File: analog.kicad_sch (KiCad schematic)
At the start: 47 parts, among them J8 Sensor harness, U7 ADS1115-Q1

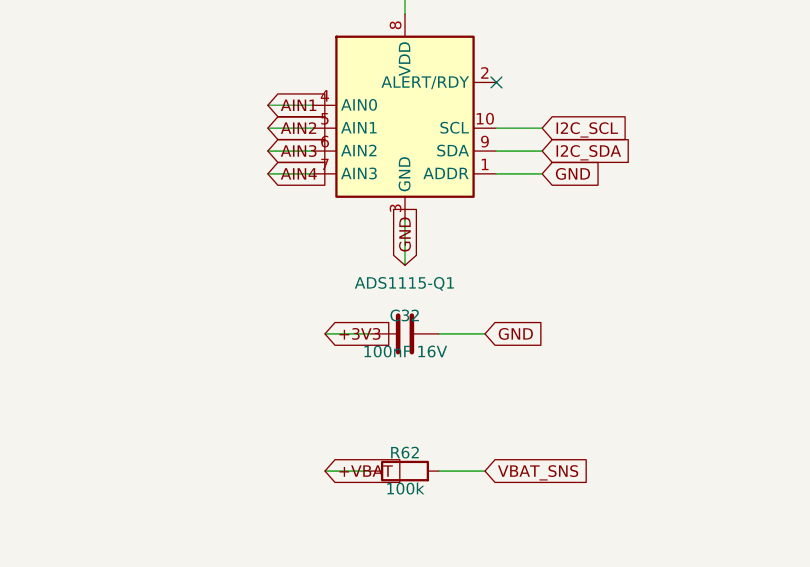
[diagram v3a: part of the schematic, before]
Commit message: Source the BOM for JLCPCB assembly; fix a nonexistent FET part number
Availability check against LCSC / DigiKey / Mouser (2026-08), with the
board now targeted at JLCPCB pick-and-place:

- Q1 was specified as PSMN4R3-100BSE, a part number that does not exist
  (Nexperia's nearest real part is the D2PAK PSMN4R8-100BSE, which would
  not fit the TO-252 footprint anyway). Replaced with Infineon
  IPD068N10N3G (LCSC C88066): DPAK, 100V, 6.8mOhm, in stock.
- LM5164QDDARQ1 is backordered at DigiKey and nearly dry at Mouser;
  switched to the non-automotive LM5164DDAR (LCSC C477928, DigiKey 3.4k
  in stock). Same silicon, minus AEC-Q100.
- ADS1115QDGSRQ1 requires a manufacturer quote at DigiKey; switched to
  ADS1115IDGSR (LCSC C37593, in stock).

README gains a sourcing table with LCSC part numbers for the critical
semiconductors and a list of what still gets picked from the live JLC
catalog at layout time (buck inductors, bulk electrolytic, 0.1%
resistors).

Validated with kicad-cli 9.0: 104 nets / 162 instances match, ERC clean.

Co-Authored-By: Claude Fable 5 <noreply@anthropic.com>
Claude-Session: https://claude.ai/code/session_01DhNbL25h25p8VFCjRfJik9
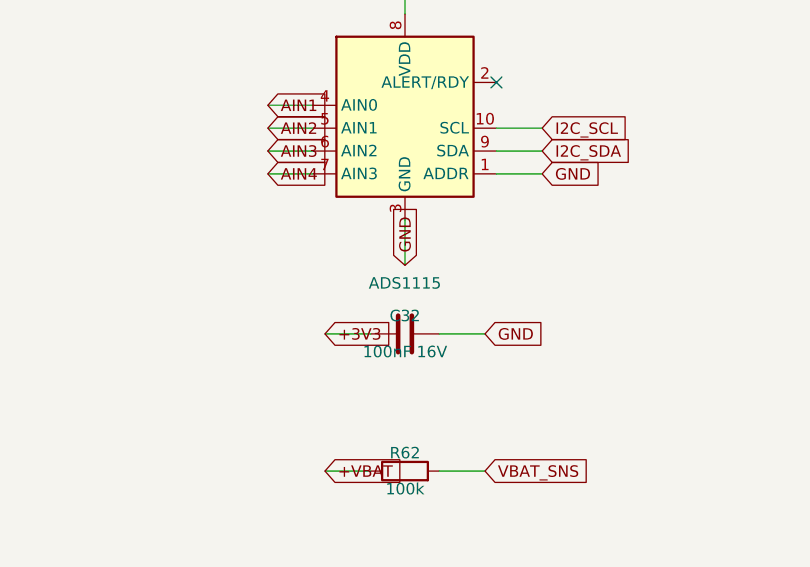
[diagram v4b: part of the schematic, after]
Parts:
- U7: value ADS1115-Q1 -> ADS1115; MPN ADS1115QDGSRQ1 -> ADS1115IDGSR
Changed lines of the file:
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@@
       (effects (font (size 1.27 1.27)) )
     )
-    (property "Value" "ADS1115-Q1" (at 241.3 209.01 0)
+    (property "Value" "ADS1115" (at 241.3 209.01 0)
       (effects (font (size 1.27 1.27)) )
     )
@@
       (effects (font (size 1.27 1.27)) hide)
     )
-    (property "MPN" "ADS1115QDGSRQ1" (at 241.3 209.01 0)
+    (property "MPN" "ADS1115IDGSR" (at 241.3 209.01 0)
       (effects (font (size 1.27 1.27)) hide)
     )

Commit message: Generate the 4-layer board: placed, DRC-clean, ready to route
gen/generate_pcb.py (runs under KiCad 9's bundled Python) builds
esp32s3-can-sd-logger.kicad_pcb from the same part/net tables as the
schematic generator: real library footprints, every pad netted, and
zone-based placement -- harness connectors on the left edge, analog
channel columns and the ESP32 with its antenna overhanging the top edge
(module keepout falls off-board), USB-C/microSD/buttons on the right,
battery front end and both bucks in the bottom band, GND and +3V3
inner-plane zones, JLC-compatible 0.2mm minimum drill.

84 x 72 mm. kicad-cli pcb drc: zero violations; the 335 unconnected
items are the unrouted ratsnest.

Also adds the project footprint library (TDK ACT45B CAN choke built from
the datasheet land pattern) and a placement render under plots/.

Co-Authored-By: Claude Fable 5 <noreply@anthropic.com>
Claude-Session: https://claude.ai/code/session_01DhNbL25h25p8VFCjRfJik9
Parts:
- J8: MPN JST B8B-PH-K -> JST B8B-PH-K-S(LF)(SN)
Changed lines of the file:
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@@
       (effects (font (size 1.27 1.27)) hide)
     )
-    (property "MPN" "JST B8B-PH-K" (at 54.61 37.56 0)
+    (property "MPN" "JST B8B-PH-K-S(LF)(SN)" (at 54.61 37.56 0)
       (effects (font (size 1.27 1.27)) hide)
     )

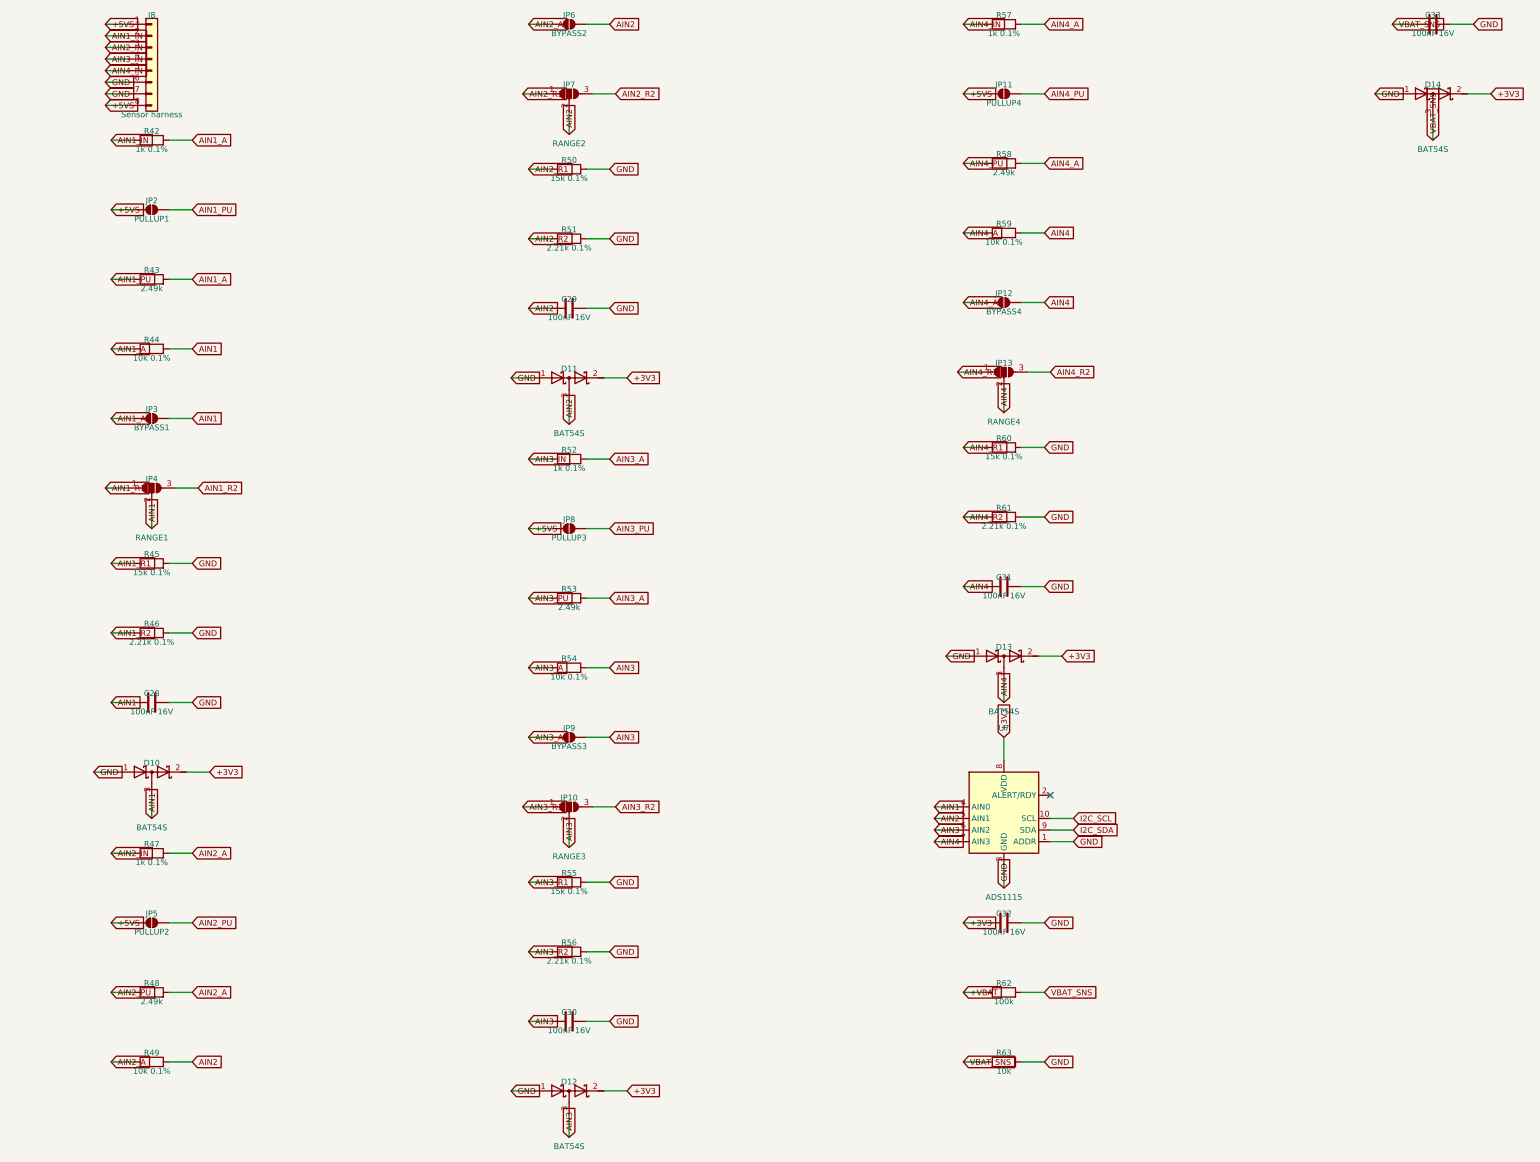
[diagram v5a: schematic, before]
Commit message: Add WS2812 5V DIN, SPI breakout, and PCB handoff docs.
Shift-light header uses a 74AHCT1G125 so GPIO48 drives real 5V data; SPI lands on IO40/41/42/47 with spare IO3/45/46 kept. README §10 covers remaining routing for the next agent.

Co-authored-by: Cursor <cursoragent@cursor.com>
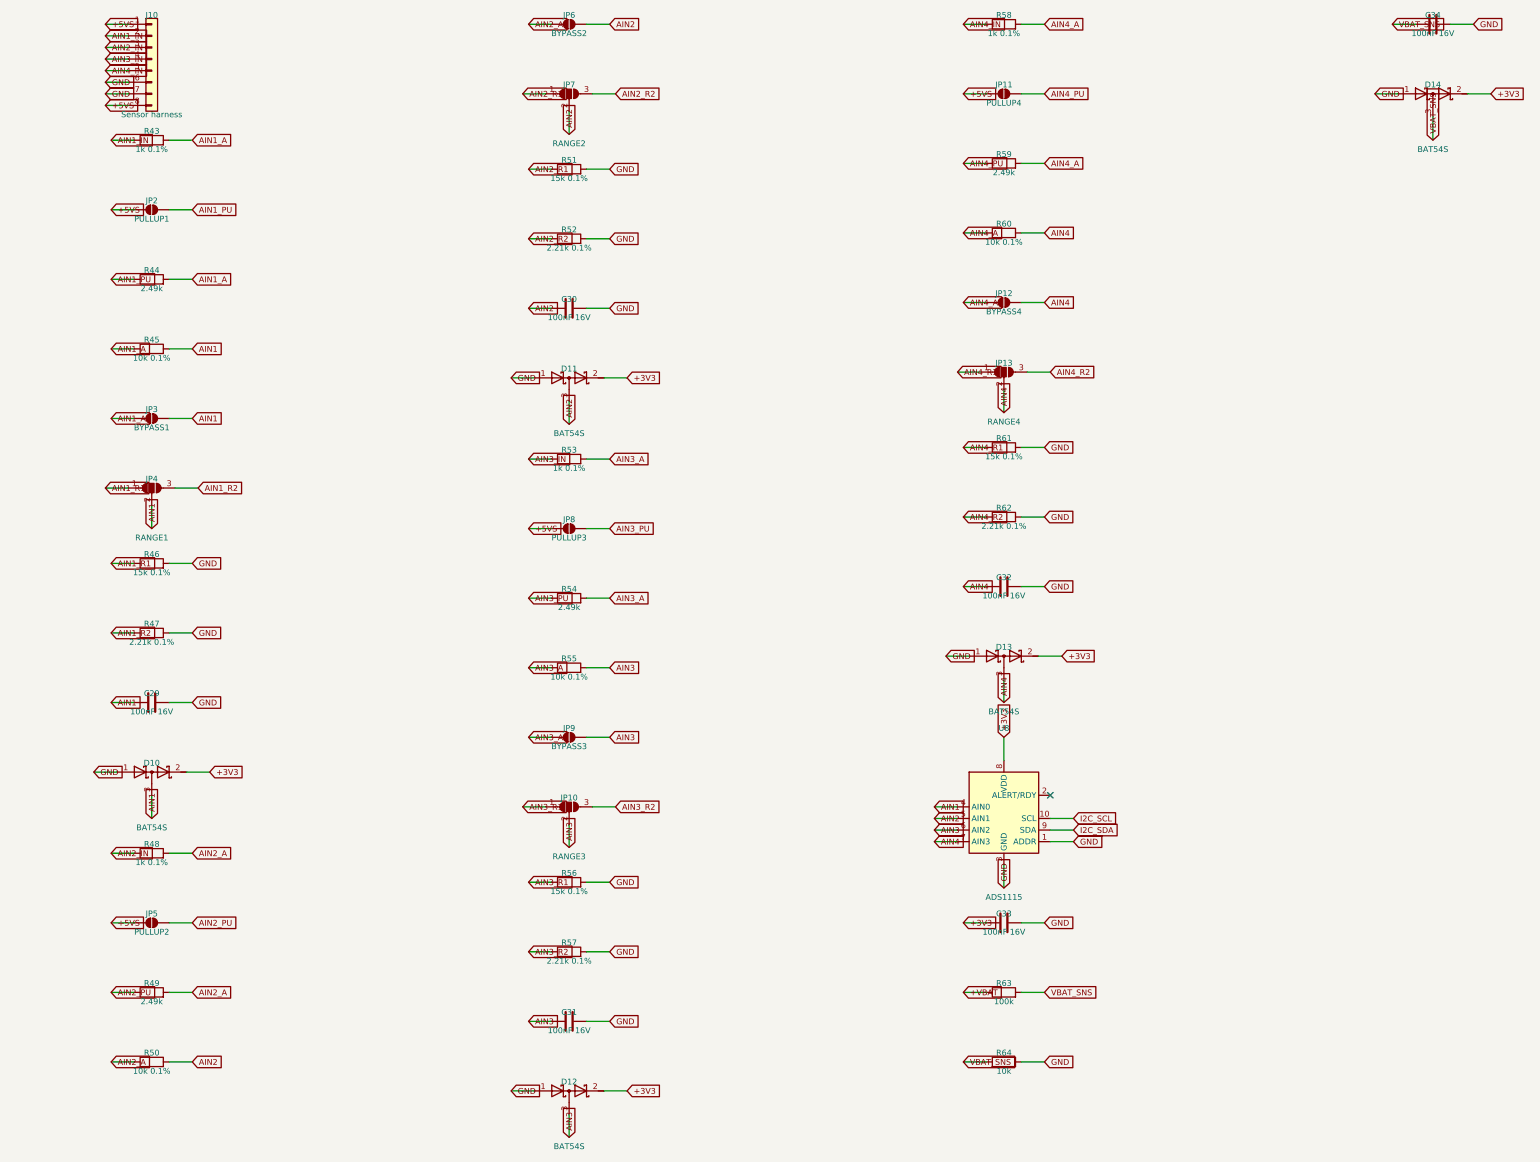
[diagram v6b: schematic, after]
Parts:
- removed C28: 100nF 16V, Capacitor_SMD:C_0805_2012Metric, symbol Device:C
- removed J8: Sensor harness, Connector_JST:JST_PH_B8B-PH-K_1x08_P2.00mm_Vertical, symbol Connector_Generic:Conn_01x08
- removed R42: 1k 0.1%, Resistor_SMD:R_0805_2012Metric, symbol Device:R
- removed U7: ADS1115, Package_SO:VSSOP-10_3x3mm_P0.5mm, symbol Analog_ADC:ADS1115IDGS
- added C34: 100nF 16V, Capacitor_SMD:C_0805_2012Metric, symbol Device:C
- added J10: Sensor harness, Connector_JST:JST_PH_B8B-PH-K_1x08_P2.00mm_Vertical, symbol Connector_Generic:Conn_01x08
- added R64: 10k, Resistor_SMD:R_0805_2012Metric, symbol Device:R
- added U8: ADS1115, Package_SO:VSSOP-10_3x3mm_P0.5mm, symbol Analog_ADC:ADS1115IDGS
- C29: Note Ch2 anti-alias / ADC charge reservoir -> Ch1 anti-alias / ADC charge reservoir
- C30: Note Ch3 anti-alias / ADC charge reservoir -> Ch2 anti-alias / ADC charge reservoir
- C31: Note Ch4 anti-alias / ADC charge reservoir -> Ch3 anti-alias / ADC charge reservoir
- C32: Note ADS1115 decoupling -> Ch4 anti-alias / ADC charge reservoir
- C33: Note (none) -> ADS1115 decoupling
- R43: value 2.49k -> 1k 0.1%; Note Ch1 bias resistor -> Ch1 series/fault-current limit; 0.1% thin film -- it is ins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
- R44: value 10k 0.1% -> 2.49k; Note Ch1 divider upper leg, 0.1% thin film for AFR-grade accuracy -> Ch1 bias resistor
- R45: value 15k 0.1% -> 10k 0.1%; Note 0-5V range: 5.0V in -> ~2.88V at the ADC (1k series include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 -> Ch1 divider upper leg, 0.1% thin film for AFR-grade accuracy
- R46, R51, R56, R61: value 2.21k 0.1% -> 15k 0.1%; Note 0-16V range: 16.0V in -> ~2.67V at the ADC (1k series inclu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 -> 0-5V range: 5.0V in -> ~2.88V at the ADC (1k series include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
- R47: value 1k 0.1% -> 2.21k 0.1%; Note Ch2 series/fault-current limit; 0.1% thin film -- it is ins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 -> 0-16V range: 16.0V in -> ~2.67V at the ADC (1k series inclu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
- R48: value 2.49k -> 1k 0.1%; Note Ch2 bias resistor -> Ch2 series/fault-current limit; 0.1% thin film -- it is ins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
- R49: value 10k 0.1% -> 2.49k; Note Ch2 divider upper leg, 0.1% thin film for AFR-grade accuracy -> Ch2 bias resistor
- R50: value 15k 0.1% -> 10k 0.1%; Note 0-5V range: 5.0V in -> ~2.88V at the ADC (1k series include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 -> Ch2 divider upper leg, 0.1% thin film for AFR-grade accuracy
- R52: value 1k 0.1% -> 2.21k 0.1%; Note Ch3 series/fault-current limit; 0.1% thin film -- it is ins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 -> 0-16V range: 16.0V in -> ~2.67V at the ADC (1k series inclu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
- R53: value 2.49k -> 1k 0.1%; Note Ch3 bias resistor -> Ch3 series/fault-current limit; 0.1% thin film -- it is ins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
- R54: value 10k 0.1% -> 2.49k; Note Ch3 divider upper leg, 0.1% thin film for AFR-grade accuracy -> Ch3 bias resistor
- R55: value 15k 0.1% -> 10k 0.1%; Note 0-5V range: 5.0V in -> ~2.88V at the ADC (1k series include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 -> Ch3 divider upper leg, 0.1% thin film for AFR-grade accuracy
- R57: value 1k 0.1% -> 2.21k 0.1%; Note Ch4 series/fault-current limit; 0.1% thin film -- it is ins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 -> 0-16V range: 16.0V in -> ~2.67V at the ADC (1k series inclu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
- R58: value 2.49k -> 1k 0.1%; Note Ch4 bias resistor -> Ch4 series/fault-current limit; 0.1% thin film -- it is ins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
- R59: value 10k 0.1% -> 2.49k; Note Ch4 divider upper leg, 0.1% thin film for AFR-grade accuracy -> Ch4 bias resistor
- R60: value 15k 0.1% -> 10k 0.1%; Note 0-5V range: 5.0V in -> ~2.88V at the ADC (1k series include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 -> Ch4 divider upper leg, 0.1% thin film for AFR-grade accuracy
- R62: value 100k -> 2.21k 0.1%; Note Battery monitor: divide by 11 -> 0-16V range: 16.0V in -> ~2.67V at the ADC (1k series inclu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
- R63: value 10k -> 100k; Note (none) -> Battery monitor: divide by 11
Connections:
- net +3V3: now also C33.1, U8.8 (VDD); no longer C32.1
- net +5VS: now also J10.1 (Pin_1), J10.8 (Pin_8)
- net +VBAT: now also R63.1; no longer R62.1
- net AIN1: now also C29.1, R45.2, U8.4 (AIN0); no longer R44.2
- net AIN1_A: now also R44.2, R45.1; no longer R44.1
- net AIN1_IN: now also R43.1, J10.2 (Pin_2)
- net AIN1_PU: now also R44.1; no longer R43.1
- net AIN1_R1: now also R46.1; no longer R45.1
- net AIN1_R2: now also R47.1; no longer R46.1
- net AIN2: now also C30.1, R50.2, U8.5 (AIN1); no longer C29.1, R49.2
- net AIN2_A: now also R49.2, R50.1; no longer R47.2, R49.1
- net AIN2_IN: now also R48.1, J10.3 (Pin_3); no longer R47.1
- net AIN2_PU: now also R49.1; no longer R48.1
- net AIN2_R1: now also R51.1; no longer R50.1
- net AIN2_R2: now also R52.1; no longer R51.1
- net AIN3: now also C31.1, R55.2, U8.6 (AIN2); no longer C30.1, R54.2
- net AIN3_A: now also R54.2, R55.1; no longer R52.2, R54.1
- net AIN3_IN: now also R53.1, J10.4 (Pin_4); no longer R52.1
- net AIN3_PU: now also R54.1; no longer R53.1
- net AIN3_R1: now also R56.1; no longer R55.1
- net AIN3_R2: now also R57.1; no longer R56.1
- net AIN4: now also C32.1, R60.2, U8.7 (AIN3); no longer C31.1, R59.2
- net AIN4_A: now also R59.2, R60.1; no longer R57.2, R59.1
- net AIN4_IN: now also R58.1, J10.5 (Pin_5); no longer R57.1
- net AIN4_PU: now also R59.1; no longer R58.1
- net AIN4_R1: now also R61.1; no longer R60.1
- net AIN4_R2: now also R62.1; no longer R61.1
- net GND: now also R47.2, R52.2, R57.2, R62.2, C34.2, J10.6 (Pin_6), J10.7 (Pin_7), R64.2, U8.1 (ADDR), U8.3 (GND); no longer R45.2, R50.2, R55.2, R60.2, R63.2
- net I2C_SCL: now also U8.10 (SCL)
- net I2C_SDA: now also U8.9 (SDA)
- net VBAT_SNS: now also R63.2, C34.1, R64.1; no longer C33.1, R62.2, R63.1
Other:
- moved on the sheet: C29, C30, C31, C32, C33, R43, R44, R45, R46, R47, R48, R49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
